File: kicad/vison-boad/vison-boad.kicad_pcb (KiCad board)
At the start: 2 copper layers, 21 parts, among them J1 USB_C_Receptacle_USB2.0, J2 Wio Terminal, J3 UART, J4 to main, SW1 BTN_UP, SW2 BTN_UP, U1 RP2040_Stamp, U2 M1n-break, U3 M1n-break, U4 M1n-break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

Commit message: no message
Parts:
- added D3: LED_PWR, 0.main.robot:LED_SMLE13WBC8W1, F.Cu at (114.4, 139.8)
- added D4: LED, 0.main.robot:LED_SMLE13WBC8W1, F.Cu at (118.8, 139.8)
- added J5: pin_test, Connector_PinHeader_2.54mm:PinHeader_1x01_P2.54mm_Vertical, F.Cu at (206.8, 74.6)
- added J6: to main, 0.main.robot:JSTB6B-ZR, F.Cu at (100.7, 128.1)
- added R8: 10k, Resistor_SMD:R_0603_1608Metric_Pad0.98x0.95mm_HandSolder, F.Cu at (136.2, 139.7)
- added R9: 10k, Resistor_SMD:R_0603_1608Metric_Pad0.98x0.95mm_HandSolder, F.Cu at (127.5, 139.7)
- added SW3: M1n_RST, Button_Switch_SMD:Panasonic_EVQPUJ_EVQPUA, F.Cu at (157.0, 119.2)
- J4: value to main -> I2C_0; footprint 0.main.robot:JSTB6B-ZR -> 0.main.robot:JSTB4B-ZR
- R2, R3: footprint Resistor_SMD:R_0603_1608Metric -> Resistor_SMD:R_0603_1608Metric_Pad0.98x0.95mm_HandSolder
- R4: value 10k -> 1K
- R7: value 10k -> 470
- SW1: value BTN_UP -> BOOTSET
- SW2: value BTN_UP -> RST
- moved R4 89.3 mm to (177.0, 107.1)
- moved R3 84.6 mm to (131.8, 139.7)
- moved R5 78.7 mm to (172.7, 106.6)
- moved U4 73.9 mm to (164.8, 73.0)
- moved J4 73.1 mm to (159.4, 113.4)
- moved R6 71.3 mm to (163.8, 113.2)
- moved D1 52.2 mm to (105.0, 140.0)
- moved R2 51.1 mm to (154.8, 123.3)
- moved U2 48.7 mm to (116.0, 73.0)
- moved U5 44.7 mm to (116.0, 106.1)
- moved SW2 41.1 mm to (181.5, 103.1)
- moved U3 38.9 mm to (140.4, 106.1)
- moved D2 37.3 mm to (109.8, 140.0)
- moved R7 30.2 mm to (123.1, 139.7)
- moved J1 15.8 mm to (96.7, 135.4)
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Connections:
- J2 pad 1: +3.3V -> unconnected-(J2-Pad1)
- J2 pad 2: unconnected-(J2-Pad2) -> +5V
- J2 pad 4: unconnected-(J2-Pad4) -> +5V
- J4 pad 1: /SCL_1 -> /SCL_0
- J4 pad 3: /SDA_1 -> /SDA_0
- J4 pad 4: +3.3V -> GND
- R4 pad 1: /SCL_1 -> Net-(D3-Pad1)
- R4 pad 2: +3.3V -> GND
- R5 pad 1: /SDA_1 -> /SCL_1
- R6 pad 1: /SCL_0 -> /SDA_1
- R7 pad 1: /SDA_0 -> Net-(D4-Pad2)
- R7 pad 2: +3.3V -> Net-(R7-Pad2)
- U1 pad 26: unconnected-(U1-Pad26) -> Net-(R7-Pad2)
- U2 pad 13: unconnected-(U2-Pad13) -> M1n_RST
- U3 pad 13: unconnected-(U3-Pad13) -> M1n_RST
- U4 pad 13: unconnected-(U4-Pad13) -> M1n_RST
- U5 pad 13: unconnected-(U5-Pad13) -> M1n_RST
- U6 pad 13: unconnected-(U6-Pad13) -> M1n_RST

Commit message: no message
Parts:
- added J7: I2C_0, 0.main.robot:JSTB4B-ZR, F.Cu at (95.7, 98.1)
- J4: value I2C_0 -> pin_test; footprint 0.main.robot:JSTB4B-ZR -> Connector_Pin:Pin_D0.7mm_L6.5mm_W1.8mm_FlatFork
- J5: value pin_test -> NEO PIXEL; footprint Connector_PinHeader_2.54mm:PinHeader_1x01_P2.54mm_Vertical -> 0.main.robot:JSTB4B-ZR
- U2, U3, U4, U5, U6: moved to B.Cu
- moved J6 124.6 mm to (205.0, 60.0)
- moved R4 116.2 mm to (63.2, 83.6)
- moved R2 111.9 mm to (50.1, 83.6)
- moved R7 98.5 mm to (44.7, 80.0)
- moved R9 98.5 mm to (49.1, 80.0)
- moved R3 95.6 mm to (54.5, 83.6)
- moved R8 95.6 mm to (58.8, 83.6)
- moved D4 92.1 mm to (45.8, 83.6)
- moved SW3 86.9 mm to (203.9, 46.0)
- moved D3 81.4 mm to (60.6, 78.6)
- moved D1 78.1 mm to (56.7, 78.6)
- moved D2 78.1 mm to (61.5, 78.6)
- moved J1 78.1 mm to (48.4, 74.0)
- moved J2 60.0 mm to (150.0, 70.0), turned to -90 degrees
- moved R5 56.9 mm to (220.0, 75.0)
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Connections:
- net /SCL_1 renamed I2C_1.SCL
- net /SDA_1 renamed I2C_1.SDA
- J3 pad 2: +5V -> +3.3V
- J4 pad 1: /SCL_0 -> GND
- J5 pad 1: GND -> unconnected-(J5-Pad1)
- R8 pad 1: /SCL_0 -> I2C_0.SCL
- R8 pad 2: +5V -> +3.3V
- R9 pad 1: /SDA_0 -> I2C_0.SDA
- R9 pad 2: +5V -> +3.3V
- U1 pad 10: /SCL_0 -> I2C_0.SCL
- U1 pad 22: unconnected-(U1-Pad22) -> NEO PIXEL
- U1 pad 34: unconnected-(U1-Pad34) -> +3.3V
- U1 pad 9: /SDA_0 -> I2C_0.SDA
- U2 pad 20: /SCL_0 -> I2C_0.SCL
- U2 pad 21: /SDA_0 -> I2C_0.SDA
- U3 pad 20: /SCL_0 -> I2C_0.SCL
- U3 pad 21: /SDA_0 -> I2C_0.SDA
- U4 pad 20: /SCL_0 -> I2C_0.SCL
- U4 pad 21: /SDA_0 -> I2C_0.SDA
- U5 pad 20: /SCL_0 -> I2C_0.SCL
- U5 pad 21: /SDA_0 -> I2C_0.SDA
- U6 pad 20: /SCL_0 -> I2C_0.SCL
- U6 pad 21: /SDA_0 -> I2C_0.SDA
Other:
- board outline added: 80 x 80 mm

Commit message: bus
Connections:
- net /USB_D+ renamed USB.D+
- net /USB_D- renamed USB.D-
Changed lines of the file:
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@@
   (net 23 "unconnected-(U1-Pad11)")
   (net 24 "unconnected-(U1-Pad12)")
-  (net 25 "/USB_D+")
-  (net 26 "/USB_D-")
+  (net 25 "USB.D+")
+  (net 26 "USB.D-")
   (net 27 "unconnected-(U1-Pad15)")
   (net 28 "unconnected-(U1-Pad16)")
@@
       (net 1 "+3.3V") (pinfunction "3.3V") (pintype "power_out"))
     (pad "35" smd rect (at 1 -11.65 270) (size 2.8 1.5) (layers "F.Cu" "F.Paste" "F.Mask")
-      (net 26 "/USB_D-") (pinfunction "USB_D-") (pintype "bidirectional"))
+      (net 26 "USB.D-") (pinfunction "USB_D-") (pintype "bidirectional"))
     (pad "36" smd rect (at -1 -11.65 270) (size 2.8 1.5) (layers "F.Cu" "F.Paste" "F.Mask")
-      (net 25 "/USB_D+") (pinfunction "USB_D+") (pintype "bidirectional"))
+      (net 25 "USB.D+") (pinfunction "USB_D+") (pintype "bidirectional"))
     (pad "37" smd rect (at -3 -11.65 270) (size 2.8 1.5) (layers "F.Cu" "F.Paste" "F.Mask")
       (net 46 "unconnected-(U1-Pad37)") (pinfunction "SWDIO") (pintype "bidirectional+no_connect"))
@@
       (net 22 "Net-(J1-PadA5)") (pinfunction "CC1") (pintype "bidirectional"))
     (pad "A6" smd rect (at -0.25 -3.67) (size 0.3 1.15) (layers "F.Cu" "F.Paste" "F.Mask")
-      (net 25 "/USB_D+") (pinfunction "D+") (pintype "bidirectional"))
+      (net 25 "USB.D+") (pinfunction "D+") (pintype "bidirectional"))
     (pad "A7" smd rect (at 0.25 -3.67) (size 0.3 1.15) (layers "F.Cu" "F.Paste" "F.Mask")
-      (net 26 "/USB_D-") (pinfunction "D-") (pintype "bidirectional"))
+      (net 26 "USB.D-") (pinfunction "D-") (pintype "bidirectional"))
     (pad "A8" smd rect (at 1.25 -3.67) (size 0.3 1.15) (layers "F.Cu" "F.Paste" "F.Mask")
       (net 43 "unconnected-(J1-PadA8)") (pinfunction "SBU1") (pintype "bidirectional+no_connect"))
@@
       (net 44 "Net-(J1-PadB5)") (pinfunction "CC2") (pintype "bidirectional"))
     (pad "B6" smd rect (at 0.75 -3.67) (size 0.3 1.15) (layers "F.Cu" "F.Paste" "F.Mask")
-      (net 25 "/USB_D+") (pinfunction "D+") (pintype "bidirectional"))
+      (net 25 "USB.D+") (pinfunction "D+") (pintype "bidirectional"))
     (pad "B7" smd rect (at -0.75 -3.67) (size 0.3 1.15) (layers "F.Cu" "F.Paste" "F.Mask")
-      (net 26 "/USB_D-") (pinfunction "D-") (pintype "bidirectional"))
+      (net 26 "USB.D-") (pinfunction "D-") (pintype "bidirectional"))
     (pad "B8" smd rect (at -1.75 -3.67) (size 0.3 1.15) (layers "F.Cu" "F.Paste" "F.Mask")
       (net 45 "unconnected-(J1-PadB8)") (pinfunction "SBU2") (pintype "bidirectional+no_connect"))
@@
     (fp_arc (start 11.1379 -1.270002) (mid 10.765926 -0.371975) (end 9.8679 -0.000002) (layer "B.SilkS") (width 0.2))
     (fp_arc (start -9.8679 -0.000002) (mid -10.765926 -0.371976) (end -11.1379 -1.270002) (layer "B.SilkS") (width 0.2))
-    (fp_arc (start 0.59659 -31.775402) (mid 1.11314 -31.672653) (end 1.551051 -31.380051) (layer "B.SilkS") (width 0.2))
+    (fp_arc (start 0.59659 -31.775402) (mid 1.113141 -31.672654) (end 1.551051 -31.380051) (layer "B.SilkS") (width 0.2))
     (fp_arc (start -11.1379 -29.768802) (mid -10.765926 -30.666828) (end -9.8679 -31.038802) (layer "B.SilkS") (width 0.2))
     (fp_circle (center 8.8773 -29.819602) (end 8.4074 -29.819602) (layer "B.SilkS") (width 0.2) (fill none))
@@
     (fp_arc (start -11.1379 -29.768802) (mid -10.765926 -30.666828) (end -9.8679 -31.038802) (layer "B.SilkS") (width 0.2))
     (fp_arc (start -9.8679 -0.000002) (mid -10.765926 -0.371976) (end -11.1379 -1.270002) (layer "B.SilkS") (width 0.2))
-    (fp_arc (start 0.59659 -31.775402) (mid 1.11314 -31.672653) (end 1.551051 -31.380051) (layer "B.SilkS") (width 0.2))
+    (fp_arc (start 0.59659 -31.775402) (mid 1.113141 -31.672654) (end 1.551051 -31.380051) (layer "B.SilkS") (width 0.2))
     (fp_arc (start 11.1379 -1.270002) (mid 10.765926 -0.371975) (end 9.8679 -0.000002) (layer "B.SilkS") (width 0.2))
     (fp_circle (center 8.8773 -29.819602) (end 8.4074 -29.819602) (layer "B.SilkS") (width 0.2) (fill none))
@@
     (fp_arc (start 2.3749 -31.038802) (mid 1.929036 -31.12749) (end 1.551051 -31.380051) (layer "B.SilkS") (width 0.2))
     (fp_arc (start -2.130146 -31.380051) (mid -1.692236 -31.672654) (end -1.175685 -31.775402) (layer "B.SilkS") (width 0.2))
-    (fp_arc (start 0.59659 -31.775402) (mid 1.11314 -31.672653) (end 1.551051 -31.380051) (layer "B.SilkS") (width 0.2))
+    (fp_arc (start 0.59659 -31.775402) (mid 1.113141 -31.672654) (end 1.551051 -31.380051) (layer "B.SilkS") (width 0.2))
     (fp_arc (start -2.130146 -31.380051) (mid -2.508131 -31.12749) (end -2.953995 -31.038802) (layer "B.SilkS") (width 0.2))
     (fp_arc (start -9.8679 -0.000002) (mid -10.765926 -0.371976) (end -11.1379 -1.270002) (layer "B.SilkS") (width 0.2))
@@
     (fp_line (start -2.95 -8.1) (end -1.93 -8.1) (layer "B.SilkS") (width 0.12))
     (fp_line (start -1.857299 -9.610603) (end -1.857299 -7.407401) (layer "B.SilkS") (width 0.2))
-    (fp_arc (start 0.59659 -31.775402) (mid 1.11314 -31.672653) (end 1.551051 -31.380051) (layer "B.SilkS") (width 0.2))
+    (fp_arc (start 0.59659 -31.775402) (mid 1.113141 -31.672654) (end 1.551051 -31.380051) (layer "B.SilkS") (width 0.2))
     (fp_arc (start -2.130146 -31.380051) (mid -2.508131 -31.12749) (end -2.953995 -31.038802) (layer "B.SilkS") (width 0.2))
     (fp_arc (start 11.1379 -1.270002) (mid 10.765926 -0.371975) (end 9.8679 -0.000002) (layer "B.SilkS") (width 0.2))
@@
     (fp_arc (start -2.130146 -31.380051) (mid -2.508131 -31.12749) (end -2.953995 -31.038802) (layer "B.SilkS") (width 0.2))
     (fp_arc (start -9.8679 -0.000002) (mid -10.765926 -0.371976) (end -11.1379 -1.270002) (layer "B.SilkS") (width 0.2))
-    (fp_arc (start 0.59659 -31.775402) (mid 1.11314 -31.672653) (end 1.551051 -31.380051) (layer "B.SilkS") (width 0.2))
+    (fp_arc (start 0.59659 -31.775402) (mid 1.113141 -31.672654) (end 1.551051 -31.380051) (layer "B.SilkS") (width 0.2))
     (fp_arc (start 2.3749 -31.038802) (mid 1.929036 -31.12749) (end 1.551051 -31.380051) (layer "B.SilkS") (width 0.2))
     (fp_arc (start 9.8679 -31.038802) (mid 10.765926 -30.666828) (end 11.1379 -29.768802) (layer "B.SilkS") (width 0.2))

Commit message: update
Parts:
- moved U6 26.6 mm to (150.0, 44.2), turned to 180 degrees
- moved U2 5.00 mm to (140.8, 90.0)
- moved U3 5.00 mm to (140.8, 120.0)
- moved U4 5.00 mm to (159.2, 90.0)
- moved U5 5.00 mm to (159.2, 120.0)

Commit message: fix: vison-boad
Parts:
- D3, J1, J3, J4, J5, J6, J7, R1, R4, SW1, SW3: moved to B.Cu
- SW2: value RST -> RESET; moved to B.Cu
- moved D4 126.6 mm to (170.0, 59.0), turned to 180 degrees
- moved R7 123.1 mm to (166.0, 59.0), turned to 180 degrees
- moved J1 119.0 mm to (150.0, 136.0), turned to 180 degrees
- moved SW3 118.0 mm to (130.0, 138.0)
- moved R2 111.1 mm to (152.0, 128.0), turned to 90 degrees
- moved R3 103.5 mm to (148.0, 128.0), turned to 90 degrees
- moved D3 91.8 mm to (150.0, 58.0)
- moved D2 91.6 mm to (153.0, 82.0), turned to 90 degrees
- moved D1 90.4 mm to (147.0, 82.0), turned to -90 degrees
- moved R4 89.5 mm to (150.0, 62.0)
- moved R1 87.9 mm to (140.0, 130.0), turned to 90 degrees
- moved R9 85.9 mm to (134.0, 67.0), turned to 180 degrees
- moved J7 83.9 mm to (175.4, 72.2), turned to -90 degrees
- moved R5 83.2 mm to (146.0, 113.0), turned to -90 degrees
- moved J5 80.5 mm to (124.5, 67.8), turned to 90 degrees
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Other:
- board size 80 x 80 mm -> 80 x 100 mm

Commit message: fix: 配線前
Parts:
- D1, D2, D4, R2, R3, R5, R6, R7, R8, R9: moved to B.Cu
- moved D4 40.0 mm to (130.0, 61.0), turned to 0 degrees
- moved R8 38.6 mm to (167.0, 50.0), turned to 0 degrees
- moved R9 35.5 mm to (167.0, 54.0), turned to 0 degrees
- moved R7 32.1 mm to (134.0, 61.0), turned to 0 degrees
- moved D2 24.0 mm to (130.0, 75.0), turned to 180 degrees
- moved R5 14.0 mm to (146.0, 99.0), turned to 90 degrees
- moved D1 13.4 mm to (135.0, 76.0)
- moved R6 12.0 mm to (150.0, 101.0), turned to 90 degrees
- moved R2 3.00 mm to (152.0, 125.0)
- moved R3 3.00 mm to (148.0, 125.0)
- moved J6 1.00 mm to (146.2, 105.5)
- moved R1 1.00 mm to (140.0, 129.0)
- moved J3 0.40 mm to (136.8, 135.9)
- turned U1 to 180 degrees
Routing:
- net USB.D+: track 0.00 -> 81.2 mm, vias 0 -> 1
- net USB.D-: track 0.00 -> 80.0 mm, vias 0 -> 3
- net GND: track 0.00 -> 20.6 mm
- net VBUS: track 0.00 -> 13.6 mm
- net Net-(J1-PadA5): track 0.00 -> 6.72 mm
- net Net-(J1-PadB5): track 0.00 -> 6.52 mm

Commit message: fix: vison-board 配線後
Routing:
- net GND: track 20.6 -> 368.0 mm
- net +5V: track 0.00 -> 225.7 mm
- net I2C_0.SDA: track 0.00 -> 213.9 mm, vias 0 -> 4
- net M1n_RST: track 0.00 -> 182.1 mm, vias 0 -> 5
- net I2C_0.SCL: track 0.00 -> 159.2 mm, vias 0 -> 4
- net +3.3V: track 0.00 -> 142.3 mm, vias 0 -> 3
- net /RESET: track 0.00 -> 120.8 mm, vias 0 -> 1
- net /RX_1: track 0.00 -> 105.0 mm, vias 0 -> 3
- net /TX_1: track 0.00 -> 101.1 mm
- net /BOOTSET: track 0.00 -> 75.3 mm, vias 0 -> 1
- net VBUS: track 13.6 -> 84.8 mm, vias 0 -> 2
- net I2C_1.SCL: track 0.00 -> 67.7 mm, vias 0 -> 1
- net I2C_1.SDA: track 0.00 -> 63.2 mm, vias 0 -> 3
- net /RX_0: track 0.00 -> 51.9 mm, vias 0 -> 2
- net /TX_0: track 0.00 -> 49.5 mm
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
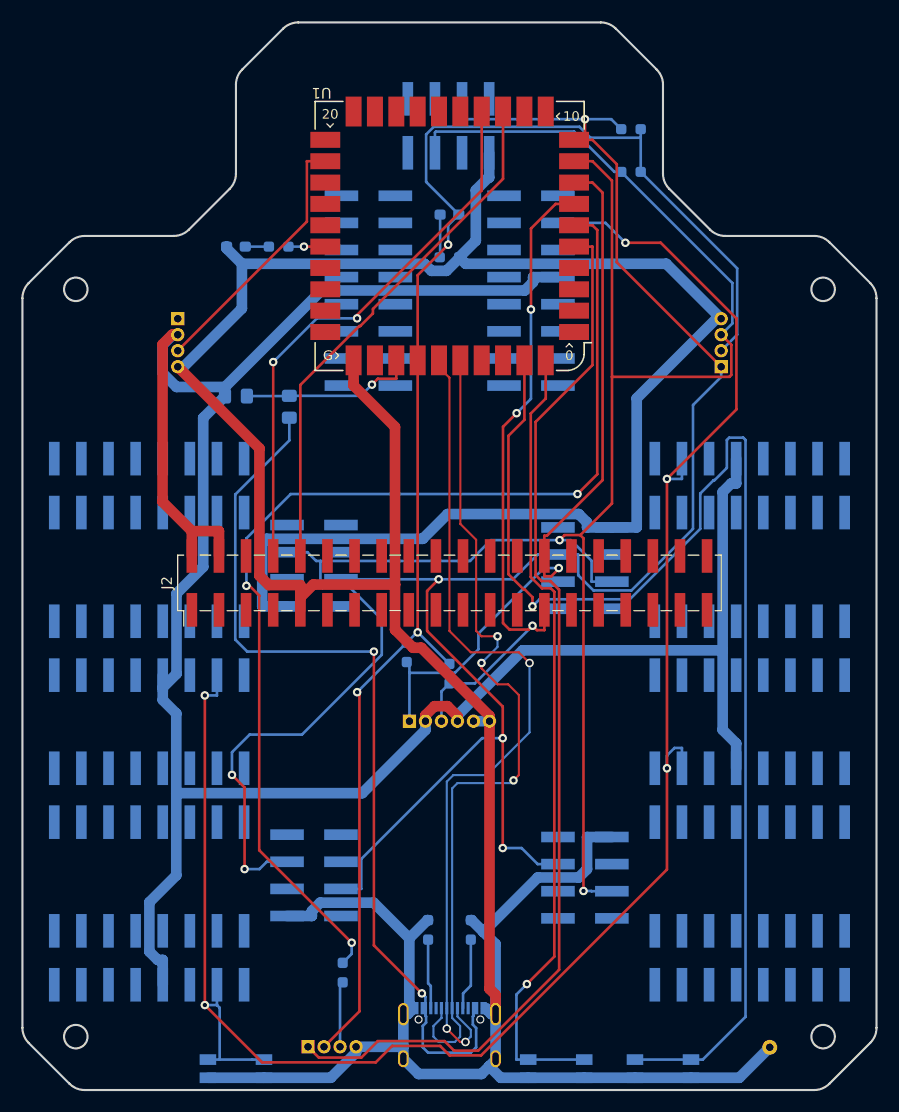
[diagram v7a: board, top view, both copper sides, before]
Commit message: add: vison-board べたGND
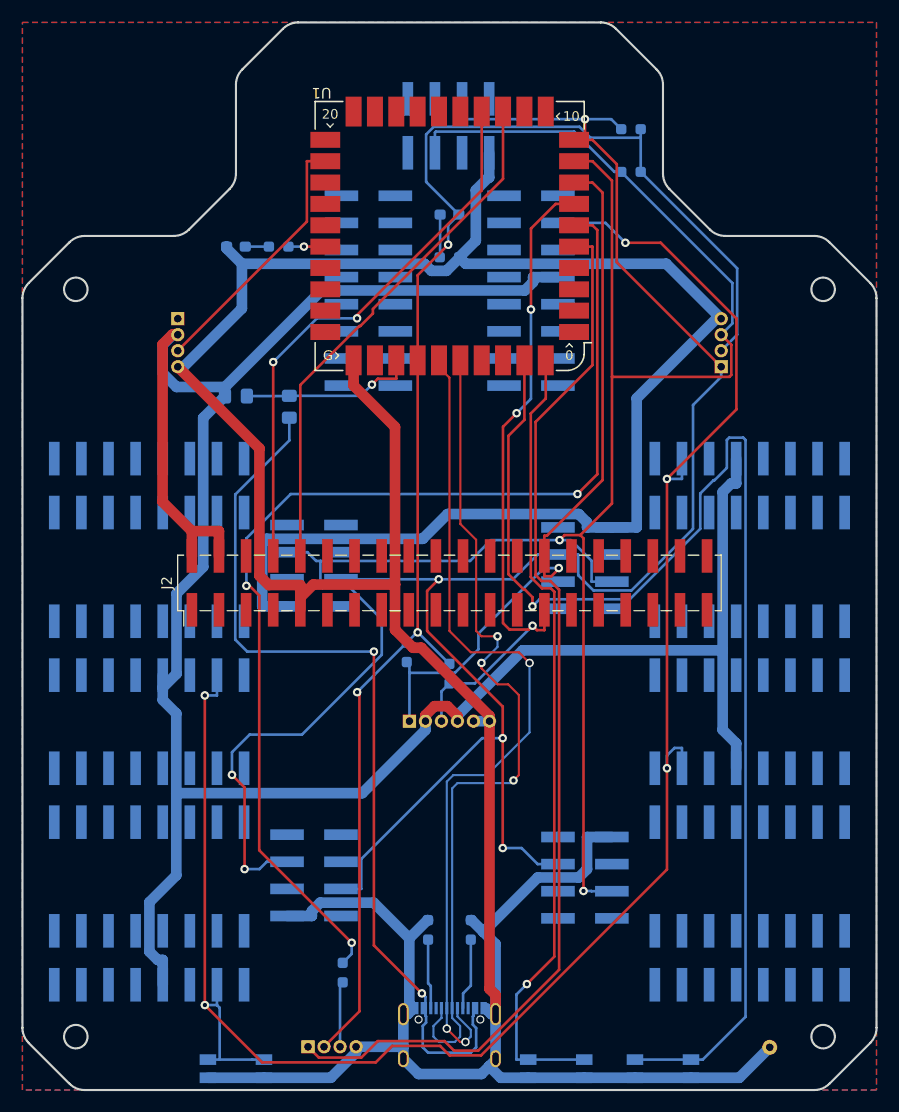
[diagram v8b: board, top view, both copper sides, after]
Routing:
- added copper zone on B.Cu, net GND
- added copper zone on F.Cu, net GND
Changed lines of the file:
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@@
     (fp_arc (start 11.1379 -1.270002) (mid 10.765926 -0.371975) (end 9.8679 -0.000002) (layer "B.SilkS") (width 0.2))
     (fp_arc (start -9.8679 -0.000002) (mid -10.765926 -0.371976) (end -11.1379 -1.270002) (layer "B.SilkS") (width 0.2))
-    (fp_arc (start 0.59659 -31.775402) (mid 1.113141 -31.672654) (end 1.551051 -31.380051) (layer "B.SilkS") (width 0.2))
+    (fp_arc (start 0.59659 -31.775402) (mid 1.11314 -31.672653) (end 1.551051 -31.380051) (layer "B.SilkS") (width 0.2))
     (fp_arc (start -11.1379 -29.768802) (mid -10.765926 -30.666828) (end -9.8679 -31.038802) (layer "B.SilkS") (width 0.2))
     (fp_circle (center 8.8773 -29.819602) (end 8.4074 -29.819602) (layer "B.SilkS") (width 0.2) (fill none))
@@
     (fp_arc (start -11.1379 -29.768802) (mid -10.765926 -30.666828) (end -9.8679 -31.038802) (layer "B.SilkS") (width 0.2))
     (fp_arc (start -9.8679 -0.000002) (mid -10.765926 -0.371976) (end -11.1379 -1.270002) (layer "B.SilkS") (width 0.2))
-    (fp_arc (start 0.59659 -31.775402) (mid 1.113141 -31.672654) (end 1.551051 -31.380051) (layer "B.SilkS") (width 0.2))
+    (fp_arc (start 0.59659 -31.775402) (mid 1.11314 -31.672653) (end 1.551051 -31.380051) (layer "B.SilkS") (width 0.2))
     (fp_arc (start 11.1379 -1.270002) (mid 10.765926 -0.371975) (end 9.8679 -0.000002) (layer "B.SilkS") (width 0.2))
     (fp_circle (center 8.8773 -29.819602) (end 8.4074 -29.819602) (layer "B.SilkS") (width 0.2) (fill none))
@@
     (fp_arc (start 2.3749 -31.038802) (mid 1.929036 -31.12749) (end 1.551051 -31.380051) (layer "B.SilkS") (width 0.2))
     (fp_arc (start -2.130146 -31.380051) (mid -1.692236 -31.672654) (end -1.175685 -31.775402) (layer "B.SilkS") (width 0.2))
-    (fp_arc (start 0.59659 -31.775402) (mid 1.113141 -31.672654) (end 1.551051 -31.380051) (layer "B.SilkS") (width 0.2))
+    (fp_arc (start 0.59659 -31.775402) (mid 1.11314 -31.672653) (end 1.551051 -31.380051) (layer "B.SilkS") (width 0.2))
     (fp_arc (start -2.130146 -31.380051) (mid -2.508131 -31.12749) (end -2.953995 -31.038802) (layer "B.SilkS") (width 0.2))
     (fp_arc (start -9.8679 -0.000002) (mid -10.765926 -0.371976) (end -11.1379 -1.270002) (layer "B.SilkS") (width 0.2))
@@
     (fp_line (start -2.95 -8.1) (end -1.93 -8.1) (layer "B.SilkS") (width 0.12))
     (fp_line (start -1.857299 -9.610603) (end -1.857299 -7.407401) (layer "B.SilkS") (width 0.2))
-    (fp_arc (start 0.59659 -31.775402) (mid 1.113141 -31.672654) (end 1.551051 -31.380051) (layer "B.SilkS") (width 0.2))
+    (fp_arc (start 0.59659 -31.775402) (mid 1.11314 -31.672653) (end 1.551051 -31.380051) (layer "B.SilkS") (width 0.2))
     (fp_arc (start -2.130146 -31.380051) (mid -2.508131 -31.12749) (end -2.953995 -31.038802) (layer "B.SilkS") (width 0.2))
     (fp_arc (start 11.1379 -1.270002) (mid 10.765926 -0.371975) (end 9.8679 -0.000002) (layer "B.SilkS") (width 0.2))
@@
     (fp_arc (start -2.130146 -31.380051) (mid -2.508131 -31.12749) (end -2.953995 -31.038802) (layer "B.SilkS") (width 0.2))
     (fp_arc (start -9.8679 -0.000002) (mid -10.765926 -0.371976) (end -11.1379 -1.270002) (layer "B.SilkS") (width 0.2))
-    (fp_arc (start 0.59659 -31.775402) (mid 1.113141 -31.672654) (end 1.551051 -31.380051) (layer "B.SilkS") (width 0.2))
+    (fp_arc (start 0.59659 -31.775402) (mid 1.11314 -31.672653) (end 1.551051 -31.380051) (layer "B.SilkS") (width 0.2))
     (fp_arc (start 2.3749 -31.038802) (mid 1.929036 -31.12749) (end 1.551051 -31.380051) (layer "B.SilkS") (width 0.2))
     (fp_arc (start 9.8679 -31.038802) (mid 10.765926 -30.666828) (end 11.1379 -29.768802) (layer "B.SilkS") (width 0.2))
@@
   (segment (start 140.7252 92.9852) (end 143.6572 95.9172) (width 0.25) (layer "B.Cu") (net 259))
   (segment (start 153.8809 88.4924) (end 151.9282 90.4451) (width 0.25) (layer "B.Cu") (net 259))
+  (zone (net 6) (net_name "GND") (layers F&B.Cu) (hatch edge 0.508)
+    (connect_pads (clearance 0.508))
+    (min_thickness 0.254) (filled_areas_thickness no)
+    (fill yes (thermal_gap 0.508) (thermal_bridge_width 0.508))
+    (polygon
+      (pts
+        (xy 190 140)
+        (xy 110 140)
+        (xy 110 40)
+        (xy 190 40)
+      )
+    )
+  )
   (group "" (id c993603e-7979-4562-85bb-0a998f89ebd4)
     (members
